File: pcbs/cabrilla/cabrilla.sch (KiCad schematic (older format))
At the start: 30 parts, among them J1 hm_1, J2 hm_2, J3 hm_3, J4 hm_4, J5 conector_entradas, J7 leds_velocidad, U4 AZ1117-3.3

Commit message: Added STM32
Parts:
- removed JP1, JP2: jumper_con1, Connector_PinHeader_2.54mm:PinHeader_1x03_P2.54mm_Vertical, symbol Device:Jumper_NC_Dual
- added D1: 1N4148, Diode_SMD:D_SOD-323F, symbol Device:D
- added J11: Conn_01x05, Connector_Molex:Molex_KK-254_AE-6410-05A_1x05_P2.54mm_Vertical, symbol Connector_Generic:Conn_01x05
- added K1: G5V-1, Relay_THT:Relay_SPDT_Omron_G5V-1, symbol Relay:G5V-1
- added Q1: PN2222A, Package_TO_SOT_SMD:SOT-23_Handsoldering, symbol Transistor_BJT:PN2222A
- added R13: 10k, Resistor_SMD:R_0805_2012Metric_Pad1.15x1.40mm_HandSolder, symbol Device:R
- added U2: STM32, elementos:STM32, symbol elementos:STM32
- 3V1: renamed from 3V3; footprint LED_SMD:LED_0805_2012Metric -> LED_SMD:LED_0805_2012Metric_Pad1.15x1.40mm_HandSolder
- 5V1: footprint LED_SMD:LED_0805_2012Metric -> LED_SMD:LED_0805_2012Metric_Pad1.15x1.40mm_HandSolder
- C2: renamed from C6; footprint Capacitor_SMD:C_0805_2012Metric -> Capacitor_SMD:C_0805_2012Metric_Pad1.15x1.40mm_HandSolder
- C3: renamed from C7; footprint Capacitor_SMD:C_0805_2012Metric -> Capacitor_SMD:C_0805_2012Metric_Pad1.15x1.40mm_HandSolder
- R1: renamed from R5; footprint Resistor_SMD:R_0805_2012Metric -> Resistor_SMD:R_0805_2012Metric_Pad1.15x1.40mm_HandSolder
- R2: renamed from R8; footprint Resistor_SMD:R_0805_2012Metric -> Resistor_SMD:R_0805_2012Metric_Pad1.15x1.40mm_HandSolder
- renumbered J7 to J1, J1 to J2, J2 to J3, J3 to J4, J4 to J5, J5 to J6, R2 to R10, R3 to R11, R4 to R12, R6 to R3, R7 to R4, 1k1 to R5, 1k2 to R6, 1k3 to R7, 1k4 to R8, R1 to R9, U4 to U1
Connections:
- net labels added: +3V3, analog_x, analog_y, freno, motor_h, motor_l, pwm_motor, reversa, reversa_signal, rx_com, rx_lcd, tx_com, tx_lcd
- net labels removed: can_opcional_1, can_opcional_2, com_1, com_2, hm, motor_out, serial_opcional_1, serial_opcional_2
- wire segments 46 -> 83
- no-connect marks 4 -> 7
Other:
- note removed: "Selector para la comunicación opcional"

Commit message: ixed
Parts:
- removed Q1: PN2222A, Package_TO_SOT_SMD:SOT-23_Handsoldering, symbol Transistor_BJT:PN2222A
- added Q1: Q_NPN_BEC, Package_TO_SOT_SMD:SOT-23_Handsoldering, symbol Device:Q_NPN_BEC
- D1: value 1N4148 -> 1N4007; footprint Diode_SMD:D_SOD-323F -> Diode_SMD:D_SMB
- J11: value Conn_01x05 -> Conn_analogo
- R1, R2, R3, R4: value 1k -> 120
- R5, R6, R7, R8: value 330 -> 120
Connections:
- net labels removed: v_pull, vin
- wire segments 83 -> 97
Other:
- note added: "Sistema para la reversa"
- moved on the sheet: D1, K1, R13, U2

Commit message: 80
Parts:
- removed J6: conector_entradas, Connector_Molex:Molex_KK-254_AE-6410-12A_1x12_P2.54mm_Vertical, symbol Connector_Generic:Conn_01x12
- added C8: 100uF, Capacitor_SMD:CP_Elec_8x6.2, symbol Device:CP
- added D2: 1N4148, Diode_SMD:D_SOD-323_HandSoldering, symbol Device:D
- added F1: 1A, Fuse:Fuse_2816_7142Metric_Pad3.20x4.45mm_HandSolder, symbol Device:Fuse
- added J12: inputs, Connector_Molex:Molex_KK-254_AE-6410-08A_1x08_P2.54mm_Vertical, symbol Connector_Generic:Conn_01x08
- added J6: Conn_analogo, Connector_Molex:Molex_KK-254_AE-6410-05A_1x05_P2.54mm_Vertical, symbol Connector_Generic:Conn_01x05
- added K2: G5V-1, Relay_THT:Relay_SPDT_Omron_G5V-1, symbol Relay:G5V-1
- added Power1: Conn_01x03, Connector_PinHeader_2.54mm:PinHeader_1x03_P2.54mm_Vertical, symbol Connector_Generic:Conn_01x03
- added Q2: Q_NPN_BEC, Package_TO_SOT_SMD:SOT-23_Handsoldering, symbol Device:Q_NPN_BEC
- added R16: 390, Resistor_SMD:R_0805_2012Metric_Pad1.15x1.40mm_HandSolder, symbol Device:R
- added R17: 10k, Resistor_SMD:R_0805_2012Metric_Pad1.15x1.40mm_HandSolder, symbol Device:R
- D1: value 1N4007 -> 1N4148; footprint Diode_SMD:D_SMB -> Diode_SMD:D_SOD-323_HandSoldering
- R1, R2: value 120 -> 1k
- R3, R4, R5, R6, R7, R8: value 120 -> 10k
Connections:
- net +3V3: now also J6.2 (Pin_2), Power1.3 (Pin_3)
- net +5V: now also D2.1 (K), F1.1, F1.2, J12.2 (Pin_2), K2.2, Power1.2 (Pin_2)
- net GND: now also C8.2, J12.1 (Pin_1), J6.1 (Pin_1), K2.1, K2.5, K2.6, Power1.1 (Pin_1), Q2.2 (E)
- net analog_x: now also U2.32 (PA7/ADC7/MOSI1/PWM); no longer U2.31 (PA6/ADC6/MISO1/PWM)
- net analog_y: now also U2.33 (PB0/ADC8); no longer U2.32 (PA7/ADC7/MOSI1/PWM)
- net freno: now also J12.6 (Pin_6), K2.10
- net hm_1: now also U2.11 (PB3/SCK1); no longer U2.30 (PA5/ADC5/SCK1)
- net hm_2: now also U2.10 (PA15/NSS1); no longer U2.29 (PA4/ADC4/NSS1)
- net hm_3: now also U2.9 (PA12/RTS1); no longer U2.26 (PA1/ADC1/RTS2/PWM)
- net hm_4: now also U2.8 (PA11/CTS1); no longer U2.25 (PA0/ADC0/CTS2/PWM)
- net led_m1: now also U2.1 (PB12/NSS2)
- net led_m2: now also U2.2 (PB13/SCK2)
- net led_m3: now also U2.3 (PB14/MISO2)
- net led_m4: now also U2.4 (PB15/MOSI2)
- net led_m5: now also U2.15 (PB7/SDA1/PWM)
- net led_m6: now also U2.16 (PB8/SCL1/PWM)
- net pwm_motor: now also C8.1, J12.4 (Pin_4), R16.1; no longer U2.34 (PB1/ADC9)
- net reversa: now also J12.5 (Pin_5)
- net freno_signal: now reaches U2.14 (PB6/SCL1/PWM)
- net freno_signal: now also R17.2
- net rx_com renamed Comunicaciones/rx_lora
- net rx_lcd renamed LCD/tx_lcd
- net tx_com renamed Comunicaciones/tx_lora
- net tx_lcd renamed LCD/rx_lcd
- new net: R16.2, U2.34 (PB1/ADC9)
- new net: D2.2 (A), K2.9, Q2.3 (C)
- new net: Q2.1 (B), R17.1
- new net analog_x2: J6.3 (Pin_3), U2.30 (PA5/ADC5/SCK1)
- new net analog_y2: J6.4 (Pin_4), U2.31 (PA6/ADC6/MISO1/PWM)
- new net corriente: J12.3 (Pin_3), U2.29 (PA4/ADC4/NSS1)
- no-connect marks 7 -> 17
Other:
- note added: "Sistema para el freno"
- moved on the sheet: 5V1, C1, R1, U2

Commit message: Updated footprints
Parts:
- C1, C8: footprint Capacitor_SMD:CP_Elec_8x6.2 -> Capacitor_SMD:CP_Elec_8x10
- F1: footprint Fuse:Fuse_2816_7142Metric_Pad3.20x4.45mm_HandSolder -> Fuse:Fuse_0201_0603Metric
- U2: symbol elementos:STM32 -> cabrilla-rescue:STM32-elementos
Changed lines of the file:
@@
 EESchema Schematic File Version 4
 LIBS:cabrilla-cache
-EELAYER 30 0
+EELAYER 29 0
 EELAYER END
 $Descr A4 11693 8268
@@
 F 0 "C1" H 6918 1096 50  0000 L CNN
 F 1 "100uF" H 6918 1005 50  0000 L CNN
-F 2 "Capacitor_SMD:CP_Elec_8x6.2" H 6838 900 50  0001 C CNN
+F 2 "Capacitor_SMD:CP_Elec_8x10" H 6838 900 50  0001 C CNN
 F 3 "~" H 6800 1050 50  0001 C CNN
 	1    6800 1050
@@
 $EndComp
 $Comp
-L elementos:STM32 U2
+L cabrilla-rescue:STM32-elementos U2
 U 1 1 5D8CD4DA
 P 3750 1900
@@
 F 0 "C8" H 7268 2696 50  0000 L CNN
 F 1 "100uF" H 7268 2605 50  0000 L CNN
-F 2 "Capacitor_SMD:CP_Elec_8x6.2" H 7188 2500 50  0001 C CNN
+F 2 "Capacitor_SMD:CP_Elec_8x10" H 7188 2500 50  0001 C CNN
 F 3 "~" H 7150 2650 50  0001 C CNN
 	1    7150 2650
@@
 F 0 "F1" V 6453 900 50  0000 C CNN
 F 1 "1A" V 6544 900 50  0000 C CNN
-F 2 "Fuse:Fuse_2816_7142Metric_Pad3.20x4.45mm_HandSolder" V 6580 900 50  0001 C CNN
+F 2 "Fuse:Fuse_0201_0603Metric" V 6580 900 50  0001 C CNN
 F 3 "~" H 6650 900 50  0001 C CNN
 	1    6650 900

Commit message: Routed
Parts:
- removed J1: leds_velocidad, Connector_Molex:Molex_KK-254_AE-6410-12A_1x12_P2.54mm_Vertical, symbol Connector_Generic:Conn_01x12
- removed R5, R6: 10k, Resistor_SMD:R_0805_2012Metric_Pad1.15x1.40mm_HandSolder, symbol Device:R
- added leds1, leds2: Conn_01x04, Connector_Molex:Molex_KK-254_AE-6410-04A_1x04_P2.54mm_Vertical, symbol Connector_Generic:Conn_01x04
- F1: footprint Fuse:Fuse_0201_0603Metric -> Fuse:Fuse_2816_7142Metric_Pad3.20x4.45mm_HandSolder
- U2: symbol cabrilla-rescue:STM32-elementos -> cabrilla-rescue:STM32-elementos-cabrilla-rescue
- renumbered J11 to analogo1, J6 to analogo2, J2 to hm1, J3 to hm2, J4 to hm3, J5 to hm4
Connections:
- net +5V: no longer F1.2, J12.2 (Pin_2)
- net GND: now also leds1.1 (Pin_1), leds1.3 (Pin_3), leds2.1 (Pin_1), leds2.3 (Pin_3)
- net analog_x: now also analogo1.4 (Pin_4); no longer analogo1.3 (Pin_3)
- net analog_y: now also analogo1.3 (Pin_3); no longer analogo1.4 (Pin_4)
- net corriente: now also J12.6 (Pin_6); no longer J12.3 (Pin_3)
- net freno: now also J12.4 (Pin_4); no longer J12.6 (Pin_6)
- net freno_signal: now also U2.11 (PB3/SCK1); no longer U2.14 (PB6/SCL1/PWM)
- net hm_1: now also U2.17 (PB9/SDA1/PWM); no longer U2.11 (PB3/SCK1)
- net hm_2: now also U2.16 (PB8/SCL1/PWM); no longer U2.10 (PA15/NSS1)
- net hm_3: now also U2.15 (PB7/SDA1/PWM); no longer U2.9 (PA12/RTS1)
- net hm_4: now also U2.14 (PB6/SCL1/PWM); no longer U2.8 (PA11/CTS1)
- net led_m3: now also R7.1
- net led_m4: now also R8.1
- net pwm_motor: now also J12.3 (Pin_3); no longer J12.4 (Pin_4)
- net reversa_signal: now also U2.10 (PA15/NSS1); no longer U2.13 (PB5/MOSI1)
- net at R8.2: now also leds2.2 (Pin_2)
- net at R3.2: now also leds1.4 (Pin_4)
- net at R7.2: now also leds2.4 (Pin_4)
- net at R4.2: now also leds1.2 (Pin_2)
- net raw_pwm: now reaches R16.2, U2.34 (PB1/ADC9)
- net VCC: now reaches J12.8 (Pin_8)
- net VCC: now also F1.2
- removed net led_m5: R7.1, U2.15 (PB7/SDA1/PWM)
- removed net led_m6: R8.1, U2.16 (PB8/SCL1/PWM)
- no-connect marks 17 -> 18
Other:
- moved on the sheet: R3, R4, R7, R8

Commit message: Final
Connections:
- net GND: now also J12.2 (Pin_2), J12.7 (Pin_7)
- no-connect marks 18 -> 16
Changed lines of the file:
@@
 	1    0    0    -1
-$EndComp
-$Comp
-L Connector_Generic:Conn_01x08 J12
-U 1 1 5D9AC376
-P 800 6350
-F 0 "J12" H 718 5725 50  0000 C CNN
-F 1 "inputs" H 718 5816 50  0000 C CNN
-F 2 "Connector_Molex:Molex_KK-254_AE-6410-08A_1x08_P2.54mm_Vertical" H 800 6350 50  0001 C CNN
-F 3 "~" H 800 6350 50  0001 C CNN
-	1    800  6350
-	-1   0    0    1
 $EndComp
 Wire Wire Line
@@
 Wire Notes Line
 	550  1600 550  5350
-NoConn ~ 1000 6050
-NoConn ~ 1000 6550
 $Comp
 L power:GND #PWR0127
@@
 NoConn ~ 3750 2600
 NoConn ~ 3750 2700
+$Comp
+L Connector_Generic:Conn_01x08 J12
+U 1 1 5D9AC376
+P 800 6350
+F 0 "J12" H 718 5725 50  0000 C CNN
+F 1 "inputs" H 718 5816 50  0000 C CNN
+F 2 "Connector_Molex:Molex_KK-254_AE-6410-08A_1x08_P2.54mm_Vertical" H 800 6350 50  0001 C CNN
+F 3 "~" H 800 6350 50  0001 C CNN
+	1    800  6350
+	-1   0    0    1
+$EndComp
+Wire Wire Line
+	1000 6550 1050 6550
+Wire Wire Line
+	1050 6550 1050 6650
+Connection ~ 1050 6650
+$Comp
+L power:GND #PWR?
+U 1 1 5D9DDC32
+P 1600 5850
+F 0 "#PWR?" H 1600 5600 50  0001 C CNN
+F 1 "GND" H 1605 5677 50  0000 C CNN
+F 2 "" H 1600 5850 50  0001 C CNN
+F 3 "" H 1600 5850 50  0001 C CNN
+	1    1600 5850
+	1    0    0    -1
+$EndComp
+Wire Wire Line
+	1000 6050 1400 6050
+Wire Wire Line
+	1400 6050 1400 5850
+Wire Wire Line
+	1400 5850 1600 5850
 $EndSCHEMATC

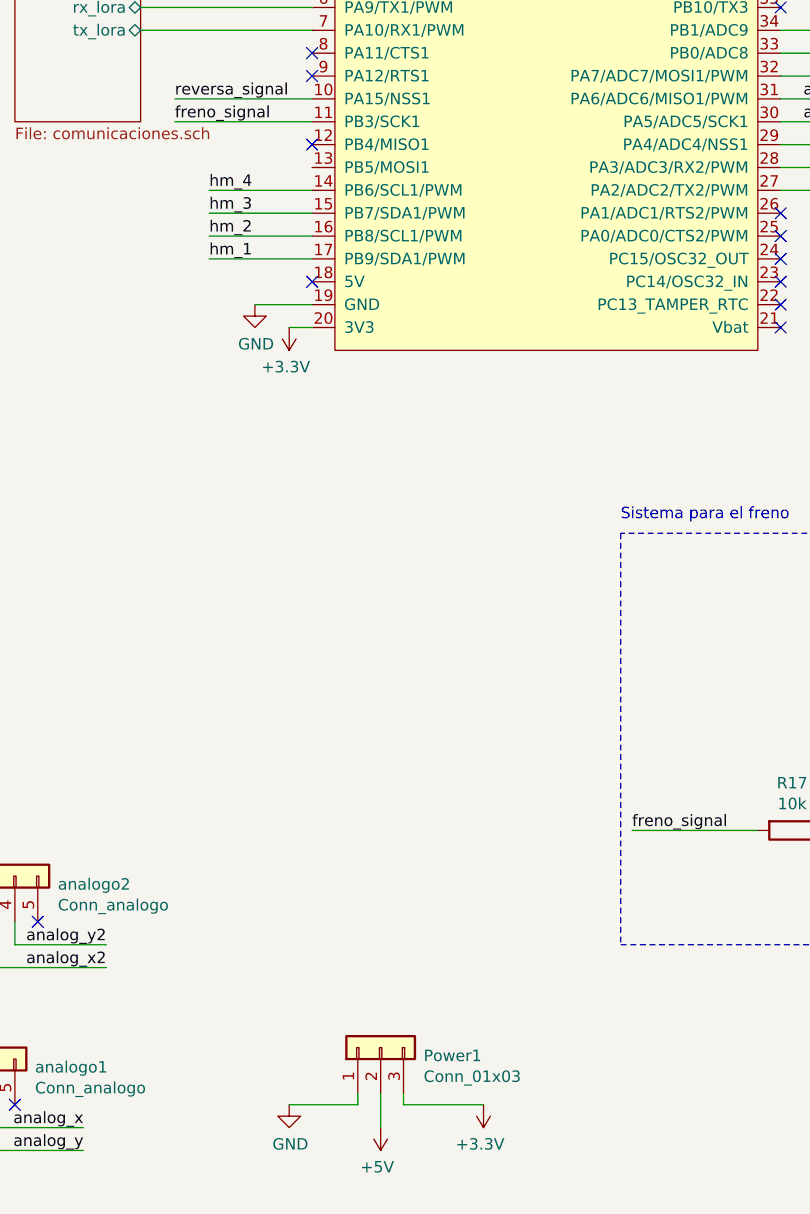
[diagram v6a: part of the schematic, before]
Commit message: Cambiados los parámetros de rutero
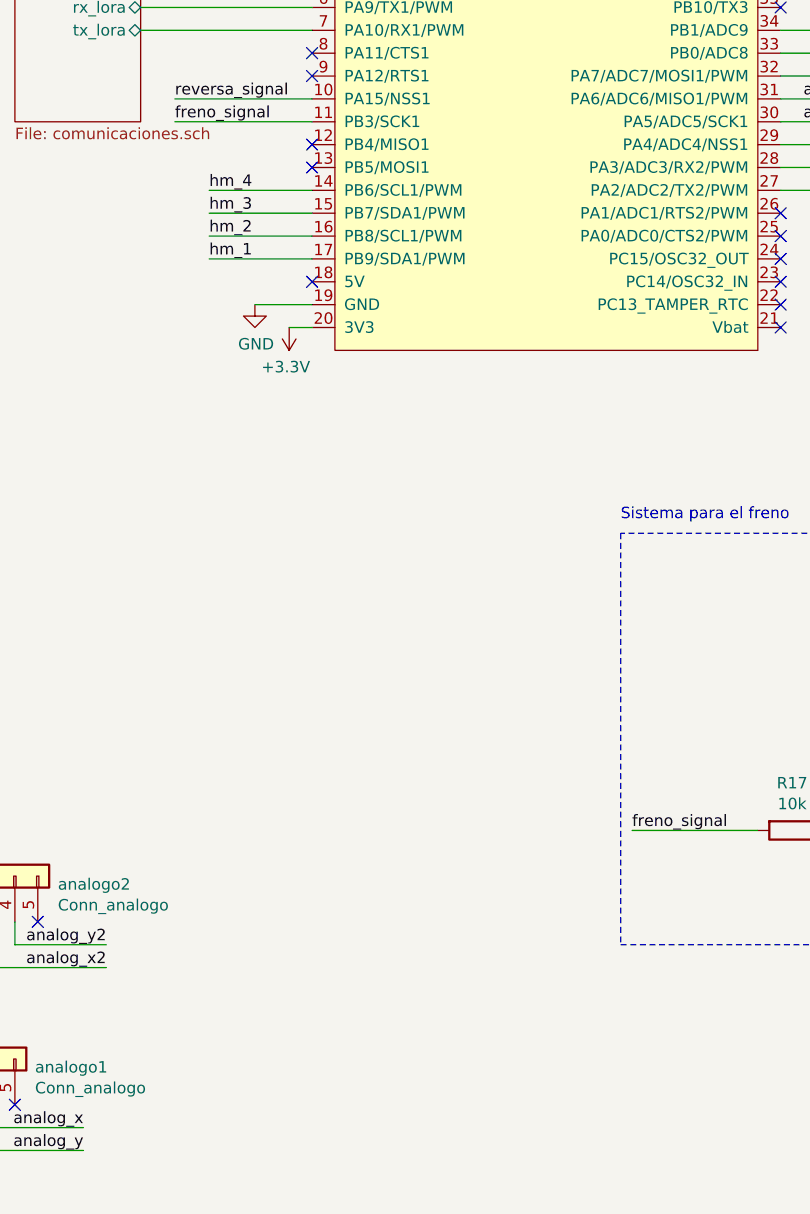
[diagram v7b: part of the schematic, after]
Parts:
- removed Power1: Conn_01x03, Connector_PinHeader_2.54mm:PinHeader_1x03_P2.54mm_Vertical, symbol Connector_Generic:Conn_01x03
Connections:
- no-connect marks 16 -> 17
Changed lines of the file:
@@
 Connection ~ 7150 2500
-$Comp
-L Connector_Generic:Conn_01x03 Power1
-U 1 1 5D9457F1
-P 4050 6950
-F 0 "Power1" V 4014 6762 50  0000 R CNN
-F 1 "Conn_01x03" V 3923 6762 50  0000 R CNN
-F 2 "Connector_PinHeader_2.54mm:PinHeader_1x03_P2.54mm_Vertical" H 4050 6950 50  0001 C CNN
-F 3 "~" H 4050 6950 50  0001 C CNN
-	1    4050 6950
-	0    -1   -1   0
-$EndComp
-Wire Wire Line
-	3950 7150 3950 7200
-Wire Wire Line
-	3950 7200 3650 7200
-Wire Wire Line
-	4050 7150 4050 7300
-Wire Wire Line
-	4150 7150 4150 7200
-Wire Wire Line
-	4150 7200 4500 7200
-$Comp
-L power:GND #PWR0119
-U 1 1 5D951608
-P 3650 7200
-F 0 "#PWR0119" H 3650 6950 50  0001 C CNN
-F 1 "GND" H 3655 7027 50  0000 C CNN
-F 2 "" H 3650 7200 50  0001 C CNN
-F 3 "" H 3650 7200 50  0001 C CNN
-	1    3650 7200
-	1    0    0    -1
-$EndComp
-$Comp
-L power:+5V #PWR0120
-U 1 1 5D951EFF
-P 4050 7300
-F 0 "#PWR0120" H 4050 7150 50  0001 C CNN
-F 1 "+5V" H 4065 7473 50  0000 C CNN
-F 2 "" H 4050 7300 50  0001 C CNN
-F 3 "" H 4050 7300 50  0001 C CNN
-	1    4050 7300
-	-1   0    0    1
-$EndComp
-$Comp
-L power:+3.3V #PWR0121
-U 1 1 5D952A86
-P 4500 7200
-F 0 "#PWR0121" H 4500 7050 50  0001 C CNN
-F 1 "+3.3V" H 4515 7373 50  0000 C CNN
-F 2 "" H 4500 7200 50  0001 C CNN
-F 3 "" H 4500 7200 50  0001 C CNN
-	1    4500 7200
-	-1   0    0    1
-$EndComp
 $Comp
 L Relay:G5V-1 K2
@@
 Connection ~ 1050 6650
 $Comp
-L power:GND #PWR?
+L power:GND #PWR0132
 U 1 1 5D9DDC32
 P 1600 5850
-F 0 "#PWR?" H 1600 5600 50  0001 C CNN
+F 0 "#PWR0132" H 1600 5600 50  0001 C CNN
 F 1 "GND" H 1605 5677 50  0000 C CNN
 F 2 "" H 1600 5850 50  0001 C CNN
@@
 Wire Wire Line
 	1400 5850 1600 5850
+NoConn ~ 3750 3100
 $EndSCHEMATC
